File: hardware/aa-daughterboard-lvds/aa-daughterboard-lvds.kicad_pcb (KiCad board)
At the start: 4 copper layers, 175.3 x 96.5 mm, 160 parts, among them CN1 Barrel_Jack, CN10 6P6C, CN11 6P6C, CN12 6P6C, CN13 6P6C, CN14 Conn_01x08, CN15 Conn_01x08, CN16 Conn_01x08, CN17 8P8C, CN18 8P8C, CN19 8P8C, CN2 Conn_01x02, CN3 Conn_01x03, CN4 Conn_01x03, CN5 6P6C, CN6 Conn_01x04, CN7 Conn_01x04, CN8 Conn_01x04, CN9 Conn_01x04, Q1 TN1610H, U1 24LC08, U2 NIS5132xx, U3 uA7805, U4 75ALS192, U5 75ALS192, U6 75ALS192, U7 75ALS192, U8 75ALS192

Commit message: Implement todos
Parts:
- removed JP1: SolderJumper_2_Open, Jumper:SolderJumper-2_P1.3mm_Bridged_RoundedPad1.0x1.5mm
- removed JP6: SolderJumper_2_Open, Jumper:SolderJumper-2_P1.3mm_Open_RoundedPad1.0x1.5mm
- added CN20: Conn_01x02, Connector_PinHeader_2.54mm:PinHeader_1x02_P2.54mm_Vertical, F.Cu at (154.9, 134.6)
- added CN21: Conn_01x02, Connector_PinHeader_2.54mm:PinHeader_1x02_P2.54mm_Vertical, F.Cu at (160.0, 134.6)
- added CN22: Conn_01x02, Connector_PinHeader_2.54mm:PinHeader_1x02_P2.54mm_Vertical, F.Cu at (165.1, 134.6)
- added CN23: Conn_01x02, Connector_PinHeader_2.54mm:PinHeader_1x02_P2.54mm_Vertical, F.Cu at (170.2, 134.6)
- added CN24: Conn_01x02, Connector_PinHeader_2.54mm:PinHeader_1x02_P2.54mm_Vertical, F.Cu at (175.3, 134.6)
- added D20: LED, LED_SMD:LED_0603_1608Metric, F.Cu at (185.9, 124.5)
- added D21: LED, LED_SMD:LED_0603_1608Metric, F.Cu at (185.9, 119.4)
- added D22: BZX79C5V1, Diode_THT:D_DO-35_SOD27_P7.62mm_Horizontal, F.Cu at (198.1, 130.8)
- added R57: 2.2k, Resistor_SMD:R_0603_1608Metric, F.Cu at (189.0, 124.5)
- added R58: 680, Resistor_SMD:R_0603_1608Metric, F.Cu at (189.0, 119.4)
- added R59: 220, Resistor_SMD:R_0603_1608Metric, F.Cu at (190.5, 128.1)
- CN3, CN4: value Conn_01x03 -> Conn_01x06; footprint Connector_PinHeader_2.54mm:PinHeader_1x03_P2.54mm_Vertical -> Connector_PinHeader_2.54mm:PinHeader_1x06_P2.54mm_Vertical
- TP1, TP10, TP11, TP12, TP13, TP14, TP15, TP16, TP17, TP18, TP19, TP2, TP20, TP21, TP22, TP23, TP24, TP25, TP26, TP27, TP28, TP29, TP3, TP30, TP31, TP4, TP5, TP6, TP7, TP8, TP9: footprint TestPoint:TestPoint_THTPad_D1.0mm_Drill0.5mm -> TestPoint:TestPoint_THTPad_D2.0mm_Drill1.0mm
- moved TP21 25.1 mm to (182.9, 119.4), turned to 270 degrees
- moved TP18 14.8 mm to (182.9, 124.5)
- moved TP6 13.0 mm to (177.8, 124.5)
- moved CN3 5.08 mm to (114.3, 129.5)
- moved CN4 5.08 mm to (149.9, 129.5)
- moved TP5 1.27 mm to (182.9, 129.5), turned to 270 degrees
- turned TP8 to 270 degrees
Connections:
- A1 pad P1_4: Net-(A1-PadP1_3) -> Net-(A1-PadP1_4)
- A1 pad P2_22: VDD -> Net-(A1-PadP2_22)
- A1 pad P2_3: Net-(A1-PadP2_3) -> +5V
- A1 pad P2_4: Net-(A1-PadP2_3) -> +5V
- CN3 pad 1: /TX_INPUT_S -> GND
- CN3 pad 2: /RX_INPUT_S -> Net-(CN3-Pad2)
- CN3 pad 3: GND -> Net-(CN3-Pad3)
- CN4 pad 1: /TX_DEBUG_S -> GND
- CN4 pad 2: /RX_DEBUG_S -> Net-(CN4-Pad2)
- CN4 pad 3: GND -> Net-(CN4-Pad3)
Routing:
- net VDD: track 193.7 -> 22.7 mm, vias 8 -> 2
- net Net-(CN1-Pad1): track 34.7 -> 11.7 mm
- net Net-(D3-Pad1): track 44.0 -> 31.1 mm, vias 0 -> 6
- net Net-(D22-Pad1): track 0.00 -> 8.40 mm
- net Net-(D2-Pad2): track 11.9 -> 18.3 mm
- net /TX_DEBUG_S: track 24.5 -> 18.3 mm, vias 0 -> 1
- net Net-(A1-PadP2_3): track 5.69 -> 0.00 mm
- net Net-(A1-PadP1_3): track 4.68 -> 0.00 mm
- net GND: track 49.3 -> 47.1 mm, vias 51 -> 53
- net /DB_SYNC_1: track 95.7 -> 94.0 mm
- net Net-(D21-Pad1): track 0.00 -> 1.50 mm
- net Net-(D20-Pad1): track 0.00 -> 1.50 mm
- net /DB_SYNC_0: track 108.0 -> 106.6 mm
- net /RX_DEBUG_S: track 24.2 -> 25.3 mm, vias 0 -> 1
- net /RX_INPUT_S: track 29.4 -> 30.5 mm
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- added copper zone on B.Cu, net Net-(CN1-Pad1)
- added copper zone on F.Cu, net Net-(CN1-Pad1)
- added copper zone on B.Cu, net Net-(D3-Pad1)
- added copper zone on F.Cu, net Net-(D3-Pad1)
- added copper zone on F.Cu, net VDD
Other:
- net class Line Drive Microstrip: via_dia 0.635 -> 0.6; via_drill 0.254 -> 0.3
- rule via_min_drill: 0.254 -> 0.3
- rule via_min_size: 0.381 -> 0.6
- board text added: "+12V"
- board text added: "1"
- board text added: "2"
- board text added: "A"
- board text added: "B"
- board text added: "CN10-13: P1,6: +5V,GND P2,5: PWM_CAP_P,N P3,4: TX_STALK_P,N"
- board text added: "CN14,15: TX_PANEL_0-7 CN16: TX_XP_0-3 Podd,even: x_P,N"
- board text added: "CN17-19: P1,2: 2_N,P P3,6: 1_N,P P4,5: 0_N,P P7,8: 3_N,P"
- board text added: "CN5: P2,5: TX, GND P3,4: GND, RX"
- board text added: "CN6-9: P1,2: TX_STALK_P,N P3,4: PWM_CAP_P,N"
- board text added: "DO NOT POP U3 IF JP6 BRIDGED"
- board text added: "X"
- board text removed: "DO NOT POPULATE U3 IF JP6 BRIDGED"

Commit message: Finish implementing daughterboard todos, except BOM on silkscreen, update library tables.
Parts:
- moved CN1 4.29 mm to (221.0, 136.2), turned to 90 degrees
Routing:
- net Net-(CN1-Pad3): track 4.52 -> 12.7 mm
- net /TX_PANEL_1: track 102.2 -> 99.9 mm, vias 4 -> 5
- net Net-(CN1-Pad1): track 11.7 -> 10.3 mm
- net /TX_PANEL_2: track 104.2 -> 103.1 mm, vias 4 -> 5
- net /TX_PANEL_7: track 21.9 -> 21.1 mm
- net /PWM_CAP_A_P: track 41.4 -> 40.7 mm
- net /PWM_CAP_1: track 102.2 -> 101.7 mm, vias 5 -> 7
- net /DB_SYNC_0: track 106.6 -> 106.2 mm, vias 0 -> 1
- net /PWM_CAP_B: track 93.9 -> 94.3 mm, vias 5 -> 7
- net /TX_PANEL_0: track 88.1 -> 88.0 mm, vias 2 -> 3
- net /DB_SYNC_1: track 94.0 -> 93.9 mm, vias 0 -> 1
- net +3V: track 108.0 -> 107.9 mm, vias 3 -> 5
- net VDD: vias 2 -> 5
- added copper zone on B.Cu, net VDD
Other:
- board text added: "AMANITA ARCADE DAUGHTERBOARD V1/2019-05-24"

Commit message: More updates to daughterboard, begin panel receiver layout
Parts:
- added CN25: Conn_01x02, Connector_Wire:SolderWirePad_1x02_P5.08mm_Drill1.5mm, F.Cu at (213.4, 134.6)
- added D23: D_Schottky, aa-daughterboard-lvds:D_SOD-128, F.Cu at (213.4, 140.2)
- added D24: D_Schottky, aa-daughterboard-lvds:D_SOD-128, F.Cu at (208.3, 140.2)
- CN2: footprint Connector_Wire:SolderWirePad_1x02_P7.62mm_Drill2.5mm -> Connector_Wire:SolderWirePad_1x02_P5.08mm_Drill1.5mm
- F1: value 3A -> 2A
- moved CN2 8.03 mm to (208.3, 134.6)
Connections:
- CN10 pad 3: /TX_STALK_1_P -> /TX_STALK_1_N
- CN10 pad 4: /TX_STALK_1_N -> /TX_STALK_1_P
- CN11 pad 3: /TX_STALK_B_P -> /TX_STALK_B_N
- CN11 pad 4: /TX_STALK_B_N -> /TX_STALK_B_P
- CN12 pad 2: /PWM_CAP_2_P -> /PWM_CAP_A_P
- CN12 pad 3: /TX_STALK_2_P -> /TX_STALK_A_N
- CN12 pad 4: /TX_STALK_2_N -> /TX_STALK_A_P
- CN12 pad 5: /PWM_CAP_2_N -> /PWM_CAP_A_N
- CN13 pad 2: /PWM_CAP_A_P -> /PWM_CAP_2_P
- CN13 pad 3: /TX_STALK_A_P -> /TX_STALK_2_N
- CN13 pad 4: /TX_STALK_A_N -> /TX_STALK_2_P
- CN13 pad 5: /PWM_CAP_A_N -> /PWM_CAP_2_N
- CN2 pad 1: Net-(CN1-Pad1) -> Net-(CN2-Pad1)
- CN8 pad 1: /TX_STALK_2_P -> /TX_STALK_A_P
- CN8 pad 2: /TX_STALK_2_N -> /TX_STALK_A_N
- CN8 pad 3: /PWM_CAP_2_P -> /PWM_CAP_A_P
- CN8 pad 4: /PWM_CAP_2_N -> /PWM_CAP_A_N
- CN9 pad 1: /TX_STALK_A_P -> /TX_STALK_2_P
- CN9 pad 2: /TX_STALK_A_N -> /TX_STALK_2_N
- CN9 pad 3: /PWM_CAP_A_P -> /PWM_CAP_2_P
- CN9 pad 4: /PWM_CAP_A_N -> /PWM_CAP_2_N
- D12 pad 1: /PWM_CAP_2_P -> /PWM_CAP_A_P
- D12 pad 3: /PWM_CAP_2_N -> /PWM_CAP_A_N
- D12 pad 4: /TX_STALK_2_P -> /TX_STALK_A_P
- D12 pad 6: /TX_STALK_2_N -> /TX_STALK_A_N
- D13 pad 1: /PWM_CAP_A_P -> /PWM_CAP_2_P
- D13 pad 3: /PWM_CAP_A_N -> /PWM_CAP_2_N
- D13 pad 4: /TX_STALK_A_P -> /TX_STALK_2_P
- D13 pad 6: /TX_STALK_A_N -> /TX_STALK_2_N
- R20 pad 2: /TX_STALK_2_P -> /TX_STALK_A_P
- R21 pad 2: /PWM_CAP_2_P -> /PWM_CAP_A_P
- R22 pad 2: /TX_STALK_A_P -> /TX_STALK_2_P
- R23 pad 2: /PWM_CAP_A_P -> /PWM_CAP_2_P
- R28 pad 2: /TX_STALK_2_N -> /TX_STALK_A_N
- R29 pad 2: /PWM_CAP_2_N -> /PWM_CAP_A_N
- R30 pad 2: /TX_STALK_A_N -> /TX_STALK_2_N
- R31 pad 2: /PWM_CAP_A_N -> /PWM_CAP_2_N
- U5 pad 1: /TX_STALK_2 -> /TX_STALK_A
- U5 pad 15: /PWM_CAP_A -> /PWM_CAP_2
- U5 pad 7: /PWM_CAP_2 -> /PWM_CAP_A
- U5 pad 9: /TX_STALK_A -> /TX_STALK_2
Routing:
- net +5V: track 66.8 -> 42.0 mm, vias 6 -> 0
- net /TX_STALK_A_P: track 36.2 -> 49.2 mm, vias 1 -> 3
- net /TX_STALK_2: track 18.2 -> 29.0 mm
- net /TX_STALK_A: track 31.7 -> 21.9 mm
- net /TX_STALK_B_P: track 36.1 -> 41.6 mm
- net /TX_STALK_2_P: track 46.8 -> 41.8 mm, vias 3 -> 1
- net /PWM_CAP_2: track 30.1 -> 25.4 mm
- net /TX_STALK_2_N: track 40.3 -> 36.9 mm, vias 1 -> 3
- net Net-(CN25-Pad1): track 0.00 -> 3.17 mm
- net Net-(CN2-Pad1): track 0.00 -> 3.17 mm
- net /TX_STALK_1_P: track 46.3 -> 49.3 mm
- net /PWM_CAP_A_P: track 40.7 -> 37.7 mm, vias 3 -> 1
- net /PWM_CAP_2_P: track 37.7 -> 40.7 mm, vias 1 -> 3
- net /TX_STALK_A_N: track 38.3 -> 41.3 mm, vias 3 -> 1
- net /PWM_CAP_A_N: track 38.8 -> 37.3 mm, vias 0 -> 2
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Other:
- board text added: "+"
- board text added: "CN10-13: P1,6: +5V,GND P2,5: PWM_CAP_P,N P3,4: TX_STALK_N,P"
- board text added: "INPUT"
- board text added: "Y"
- board text added: "Z"
- board text removed: "CN10-13: P1,6: +5V,GND P2,5: PWM_CAP_P,N P3,4: TX_STALK_P,N"

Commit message: Update to use a shared schematic component/footprint library
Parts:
- A1: footprint aa-daughterboard-lvds:STM32F407_Discovery_P1_P2_Socket -> aa-shared:STM32F407_Discovery_P1_P2_Socket
- CN10, CN11, CN12, CN13, CN5: footprint aa-daughterboard-lvds:6P6C_Assmann_A-2014-1-4 -> aa-shared:6P6C_Assmann_A-2014-1-4
- CN17, CN18, CN19: footprint aa-daughterboard-lvds:8P8C_Assmann_A-2014-2S-4 -> aa-shared:8P8C_Assmann_A-2014-2S-4
- D23, D24: footprint aa-daughterboard-lvds:D_SOD-128 -> aa-shared:D_SOD-128
- D3: footprint aa-daughterboard-lvds:D_SOD-923 -> aa-shared:D_SOD-923
- F1: footprint aa-daughterboard-lvds:Fuseholder_Clip_5x20_Bel_FC-211-22 -> aa-shared:Fuseholder_Clip_5x20_Bel_FC-211-22
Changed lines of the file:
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@@
     (add_net "Net-(A1-PadP1_3)")
   )
-  (module aa-daughterboard-lvds:6P6C_Assmann_A-2014-1-4 (layer F.Cu)
+  (module aa-shared:6P6C_Assmann_A-2014-1-4 (layer F.Cu)
     (at 205.74 86.36 90)
     (descr http://www.assmann-wsw.com/fileadmin/datasheets/ASS_7327_CO.pdf)
@@
     )
   )
-  (module aa-daughterboard-lvds:6P6C_Assmann_A-2014-1-4 (layer F.Cu)
+  (module aa-shared:6P6C_Assmann_A-2014-1-4 (layer F.Cu)
     (at 205.74 104.14 90)
     (descr http://www.assmann-wsw.com/fileadmin/datasheets/ASS_7327_CO.pdf)
@@
       (net 1 GND) (thermal_width 1.016))
   )
-  (module aa-daughterboard-lvds:D_SOD-128 (layer F.Cu)
+  (module aa-shared:D_SOD-128 (layer F.Cu)
     (at 213.36 140.208 90)
     (descr SOD-123)
@@
     )
   )
-  (module aa-daughterboard-lvds:D_SOD-128 (layer F.Cu)
+  (module aa-shared:D_SOD-128 (layer F.Cu)
     (at 208.28 140.208 90)
     (descr SOD-123)
@@
     )
   )
-  (module aa-daughterboard-lvds:STM32F407_Discovery_P1_P2_Socket (layer F.Cu)
+  (module aa-shared:STM32F407_Discovery_P1_P2_Socket (layer F.Cu)
     (at 116.84 58.42)
     (descr "Through hole straight socket strip, 2x25, 2.54mm pitch, double cols (from Kicad 4.0.7), script generated")
@@
     )
   )
-  (module aa-daughterboard-lvds:8P8C_Assmann_A-2014-2S-4 (layer F.Cu)
+  (module aa-shared:8P8C_Assmann_A-2014-2S-4 (layer F.Cu)
     (at 76.2 63.5 270)
     (descr http://www.assmann-wsw.com/fileadmin/datasheets/ASS_7330_CO.pdf)
@@
     )
   )
-  (module aa-daughterboard-lvds:6P6C_Assmann_A-2014-1-4 (layer F.Cu)
+  (module aa-shared:6P6C_Assmann_A-2014-1-4 (layer F.Cu)
     (at 205.74 68.58 90)
     (descr http://www.assmann-wsw.com/fileadmin/datasheets/ASS_7327_CO.pdf)
@@
     )
   )
-  (module aa-daughterboard-lvds:8P8C_Assmann_A-2014-2S-4 (layer F.Cu)
+  (module aa-shared:8P8C_Assmann_A-2014-2S-4 (layer F.Cu)
     (at 76.2 85.09 270)
     (descr http://www.assmann-wsw.com/fileadmin/datasheets/ASS_7330_CO.pdf)
@@
     )
   )
-  (module aa-daughterboard-lvds:6P6C_Assmann_A-2014-1-4 (layer F.Cu)
+  (module aa-shared:6P6C_Assmann_A-2014-1-4 (layer F.Cu)
     (at 121.92 129.54)
     (descr http://www.assmann-wsw.com/fileadmin/datasheets/ASS_7327_CO.pdf)
@@
     )
   )
-  (module aa-daughterboard-lvds:6P6C_Assmann_A-2014-1-4 (layer F.Cu)
+  (module aa-shared:6P6C_Assmann_A-2014-1-4 (layer F.Cu)
     (at 205.74 121.92 90)
     (descr http://www.assmann-wsw.com/fileadmin/datasheets/ASS_7327_CO.pdf)
@@
     )
   )
-  (module aa-daughterboard-lvds:8P8C_Assmann_A-2014-2S-4 (layer F.Cu)
+  (module aa-shared:8P8C_Assmann_A-2014-2S-4 (layer F.Cu)
     (at 76.2 106.68 270)
     (descr http://www.assmann-wsw.com/fileadmin/datasheets/ASS_7330_CO.pdf)
@@
     )
   )
-  (module aa-daughterboard-lvds:D_SOD-923 (layer B.Cu)
+  (module aa-shared:D_SOD-923 (layer B.Cu)
     (at 175.006 144.018 270)
     (descr SOD-323)
@@
     )
   )
-  (module aa-daughterboard-lvds:Fuseholder_Clip_5x20_Bel_FC-211-22 (layer F.Cu)
+  (module aa-shared:Fuseholder_Clip_5x20_Bel_FC-211-22 (layer F.Cu)
     (at 178.689 142.24)
     (tags "fuse clip 5x20")

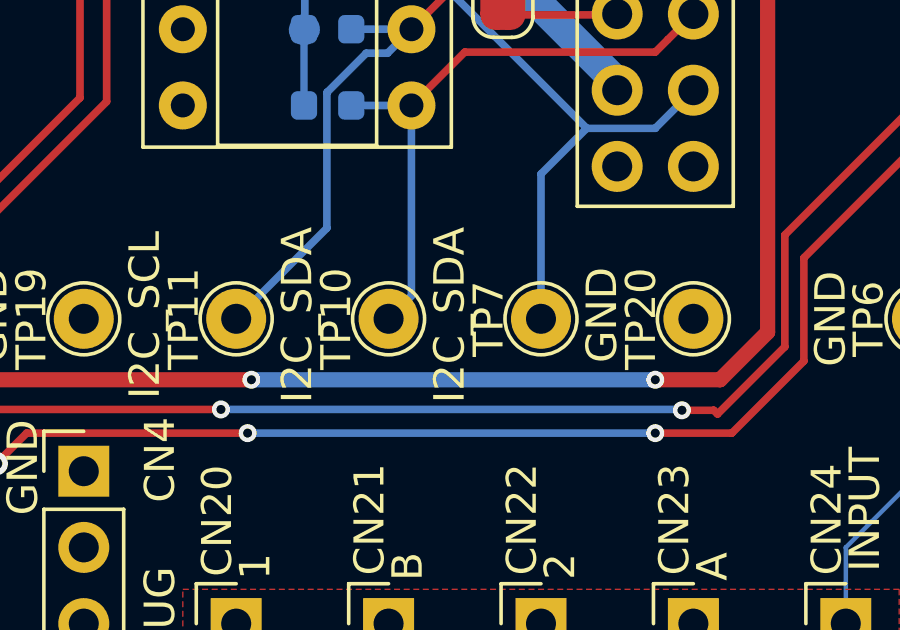
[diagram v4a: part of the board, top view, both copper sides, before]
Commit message: Fix bad test point label
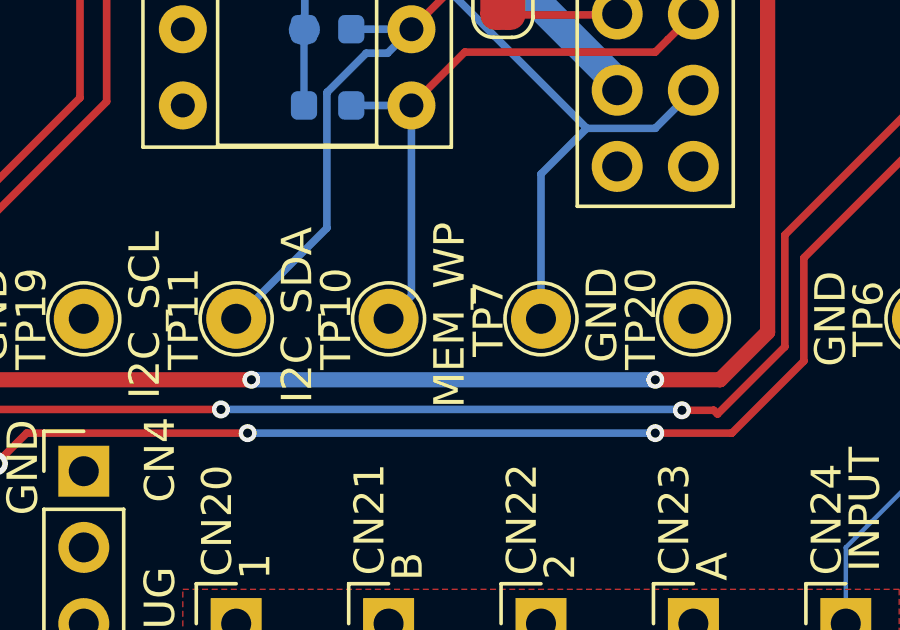
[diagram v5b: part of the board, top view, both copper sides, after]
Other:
- board text added: "MEM_WP"

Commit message: Substantial rework of system, new layouts done for daughterboard, power, stalk receiver
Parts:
- removed CN20, CN21, CN22, CN23, CN24: Conn_01x02, Connector_PinHeader_2.54mm:PinHeader_1x02_P2.54mm_Vertical
- removed CN25: Conn_01x02, Connector_Wire:SolderWirePad_1x02_P5.08mm_Drill1.5mm
- removed D2: BZX79C15, Diode_THT:D_DO-35_SOD27_P7.62mm_Horizontal
- removed D22: BZX79C5V1, Diode_THT:D_DO-35_SOD27_P7.62mm_Horizontal
- removed D23, D24: D_Schottky, aa-shared:D_SOD-128
- removed JP4: SolderJumper_3_Bridged12, Jumper:SolderJumper-3_P1.3mm_Bridged2Bar12_RoundedPad1.0x1.5mm
- removed Q1: TN1610H, Package_TO_SOT_THT:TO-220-3_Vertical
- removed R1, R59: 220, Resistor_SMD:R_0603_1608Metric
- removed R5: 10k, Resistor_SMD:R_0603_1608Metric
- added F2: 0.5A, Fuse:Fuse_0603_1608Metric, F.Cu at (203.5, 124.4)
- added F3: 0.5A, Fuse:Fuse_0603_1608Metric, F.Cu at (203.5, 106.8)
- added F4: 0.5A, Fuse:Fuse_0603_1608Metric, F.Cu at (203.5, 89.2)
- added F5: 0.5A, Fuse:Fuse_0603_1608Metric, F.Cu at (203.5, 71.0)
- added TP32: TestPoint, TestPoint:TestPoint_THTPad_D2.0mm_Drill1.0mm, F.Cu at (167.6, 142.2)
- C1: value 10n -> 100u; footprint Capacitor_SMD:C_0603_1608Metric -> Capacitor_THT:CP_Radial_D10.0mm_P2.50mm_P5.00mm
- C2, C3, D3, R10, R12, R56: moved to F.Cu
- F1: value 2A -> 0.5A
- moved TP18 81.4 mm to (102.9, 139.7)
- moved TP31 54.8 mm to (172.7, 142.2), turned to 0 degrees
- moved TP19 44.6 mm to (108.0, 139.7)
- moved TP30 42.6 mm to (177.8, 142.2), turned to 0 degrees
- moved D3 36.1 mm to (210.7, 138.7)
- moved TP21 33.4 mm to (149.9, 124.5)
- moved TP28 30.2 mm to (108.0, 134.6)
- moved R58 27.6 mm to (167.6, 136.9), turned to 0 degrees
- moved D21 26.5 mm to (167.6, 138.6)
- moved JP5 21.5 mm to (193.5, 140.5)
- moved R15 21.5 mm to (192.8, 141.5)
- moved U2 21.5 mm to (195.8, 141.0)
- moved TP6 20.5 mm to (188.0, 142.2), turned to 0 degrees
- moved D20 19.3 mm to (172.7, 138.6)
- moved R57 19.3 mm to (175.8, 138.6)
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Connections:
- A1 pad P2_31: Net-(A1-PadP2_31) -> /DB_SYNC_3
- A1 pad P2_34: Net-(A1-PadP2_34) -> /DB_SYNC_2
- A1 pad P2_43: Net-(A1-PadP2_43) -> /I2C_SCL
- C4 pad 1: VDD -> Net-(C4-Pad1)
- CN1 pad 1: Net-(CN1-Pad1) -> Net-(C1-Pad1)
- CN10 pad 1: +5V -> Net-(CN10-Pad1)
- CN10 pad 2: /PWM_CAP_1_P -> /TX_STALK_1_P
- CN10 pad 4: /TX_STALK_1_P -> /PWM_CAP_1_P
- CN11 pad 1: +5V -> Net-(CN11-Pad1)
- CN11 pad 2: /PWM_CAP_B_P -> /TX_STALK_B_P
- CN11 pad 4: /TX_STALK_B_P -> /PWM_CAP_B_P
- CN12 pad 1: +5V -> Net-(CN12-Pad1)
- CN12 pad 2: /PWM_CAP_A_P -> /TX_STALK_A_P
- CN12 pad 4: /TX_STALK_A_P -> /PWM_CAP_A_P
- CN13 pad 1: +5V -> Net-(CN13-Pad1)
- CN13 pad 2: /PWM_CAP_2_P -> /TX_STALK_2_P
- CN13 pad 4: /TX_STALK_2_P -> /PWM_CAP_2_P
- CN2 pad 1: Net-(CN2-Pad1) -> Net-(C1-Pad1)
- D20 pad 2: VDD -> Net-(C4-Pad1)
- D3 pad 1: Net-(D3-Pad1) -> Net-(C1-Pad1)
- F1 pad 1: Net-(D3-Pad1) -> Net-(C4-Pad1)
- F1 pad 2: Net-(CN1-Pad1) -> +12V
- JP5 pad 1: Net-(D3-Pad1) -> Net-(C1-Pad1)
- JP5 pad 2: VDD -> +12V
- JP7 pad 1: VDD -> Net-(C4-Pad1)
- R15 pad 2: VDD -> +12V
- R56 pad 1: Net-(CN1-Pad1) -> Net-(C1-Pad1)
- TP18 pad 1: VDD -> /DB_SYNC_2
- TP19 pad 1: GND -> /DB_SYNC_3
- TP21 pad 1: +5V -> GND
- TP30 pad 1: Net-(CN1-Pad1) -> +12V
- TP31 pad 1: GND -> Net-(C4-Pad1)
- TP5 pad 1: Net-(D3-Pad1) -> GND
- TP6 pad 1: GND -> Net-(C1-Pad1)
- U2 pad 10: VDD -> +12V
- U2 pad 11: Net-(D3-Pad1) -> Net-(C1-Pad1)
- U2 pad 6: VDD -> +12V
- U2 pad 7: VDD -> +12V
- U2 pad 8: VDD -> +12V
- U2 pad 9: VDD -> +12V
- U3 pad 1: VDD -> Net-(C4-Pad1)
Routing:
- net /DB_SYNC_2: track 0.00 -> 97.4 mm, vias 0 -> 3
- net /DB_SYNC_3: track 0.00 -> 92.5 mm, vias 0 -> 3
- net +12V: track 0.00 -> 41.6 mm, vias 0 -> 3
- net Net-(C4-Pad1): track 0.00 -> 40.7 mm
- net Net-(D3-Pad1): track 31.1 -> 0.00 mm, vias 6 -> 0
- net VDD: track 22.7 -> 0.00 mm, vias 5 -> 0
- net Net-(D2-Pad2): track 18.3 -> 0.00 mm
- net Net-(CN1-Pad1): track 10.3 -> 0.00 mm, vias 20 -> 0
- net Net-(D22-Pad1): track 8.40 -> 0.00 mm
- net Net-(CN1-Pad3): track 12.7 -> 5.56 mm
- net +5V: track 42.0 -> 48.1 mm
- net /TX_STALK_2_P: track 41.8 -> 37.1 mm
- net GND: track 46.9 -> 51.6 mm, vias 53 -> 60
- net /RX_DEBUG_S: track 25.3 -> 29.5 mm
- net /TX_STALK_B_P: track 41.6 -> 37.4 mm
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- added copper zone on F.Cu, net +12V
- added copper zone on B.Cu, net Net-(C1-Pad1)
- added copper zone on F.Cu, net Net-(C1-Pad1)
- removed copper zone on B.Cu, net Net-(CN1-Pad1)
- removed copper zone on F.Cu, net Net-(CN1-Pad1)
- removed copper zone on B.Cu, net Net-(D3-Pad1)
- removed copper zone on F.Cu, net Net-(D3-Pad1)
- removed copper zone on B.Cu, net VDD
- removed copper zone on F.Cu, net VDD
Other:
- board text added: "+12V FUSED"
- board text added: "AMANITA ARCADE DAUGHTERBOARD V2/2019-06-15"
- board text added: "BRIDGE JP7 FOR +5V VIN DO NOT POPULATE U3"
- board text added: "CN"
- board text added: "CN10-13: P1,6: +5V,GND P2,3: PWM_CAP_P,N P4,5: TX_STALK_N,P"
- board text added: "CP"
- board text added: "PD2"
- board text added: "PD3"
- board text added: "PN"
- board text added: "SN"
- board text added: "SP"
- board text added: "SYNC2 MISC"
- board text added: "SYNC3 MISC"
- board text added: "TX/RX_INPUT"
- board text added: "VIN"
- board text removed: "AMANITA ARCADE DAUGHTERBOARD V1/2019-05-24"
- board text removed: "BRIDGE JP6 TO USE +5V FROM STM32F4 DISCOVERY BOARD A1 DO NOT POPULATE U3"
- board text removed: "BRIDGE JP7 TO CONNECT VDD AND +5V POWER INPUT MUST BE REGULATED DO NOT POPULATE U3"
- board text removed: "CN10-13: P1,6: +5V,GND P2,5: PWM_CAP_P,N P3,4: TX_STALK_N,P"
- board text removed: "CN5, CN3 TX/RX_INPUT"
- board text removed: "CUT JP1 IF STM32F4 DISCOVERY BOARD A1 IS INDEPENDENTLY POWERED"
- board text removed: "DO NOT POP U3 IF JP6 BRIDGED"
- board text removed: "DO NOT POPULATE Q1 IF F1 BRIDGED"
- board text removed: "INPUT"
- board text removed: "JP4 SELECTS I2C_SCL DEFAULT IS PA8 CUT 1-2, BRIDGE 2-3 TO SELECT PC8"
- board text removed: "VSUPPLY"
- board text removed: "VSUPPLY FUSED"
